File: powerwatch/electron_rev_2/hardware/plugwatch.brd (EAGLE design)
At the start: 57.1 x 93 mm, 111 parts, among them J1 TC2030-JLINK-NL, J2 DM3AT-SF-PEJM5, SW1 SIP3240X, SW2 SIP3240X, SW3 SIP3240X, SW4 SIP3240X, SW7 SIP3240X, U1 MAX-M8, U3 ISL29035, U37 MPU-9250, U4 NRF51822QF, U5 SAFFB1G56KB0F0A, U6 BGA725L6-ALT, U7 OPA322AIDBVT, U8 MAX740XESA, X3 16MHz, X4 ABS05-32.768KHZ-9-T

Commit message: Fixed a schematic boo boo
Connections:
- removed net BLE_VCC: R13.1
- net VCC_BLE: now also R13.1
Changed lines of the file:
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@@
 <wire x1="18.038" y1="9.361" x2="16.727" y2="9.361" width="0.4064" layer="16"/>
 <wire x1="16.727" y1="9.361" x2="16.51" y2="9.144" width="0.4064" layer="16"/>
+<contactref element="R13" pad="1"/>
+<wire x1="16.51" y1="13.716" x2="16.28013125" y2="15.0876" width="0" layer="19" extent="16-16"/>
 </signal>
 <signal name="N$14">
@@
 <wire x1="25.4" y1="36.576" x2="28.575" y2="33.401" width="0.254" layer="1"/>
 </signal>
-<signal name="BLE_VCC">
-<contactref element="R13" pad="1"/>
-</signal>
 <signal name="GND2">

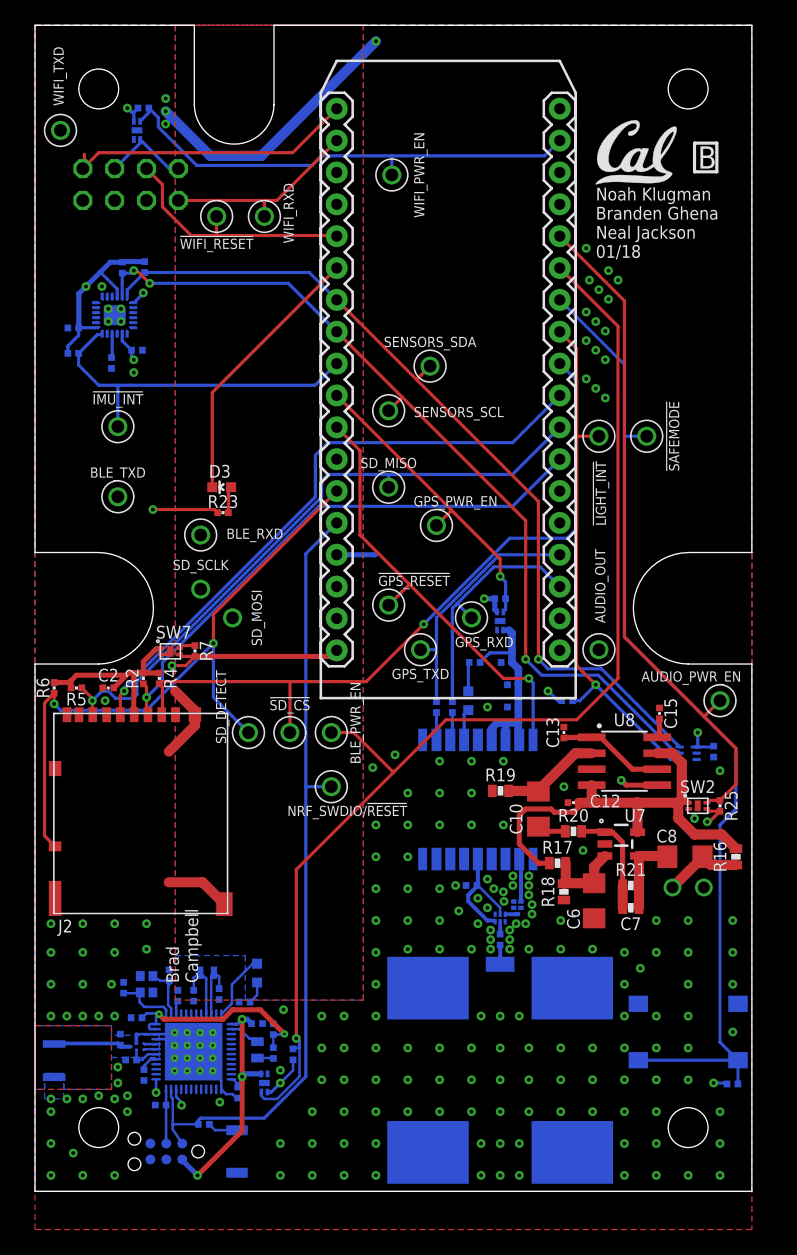
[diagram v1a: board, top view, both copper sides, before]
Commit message: Fix BLE VCC, testpoints, labels, relabel parts
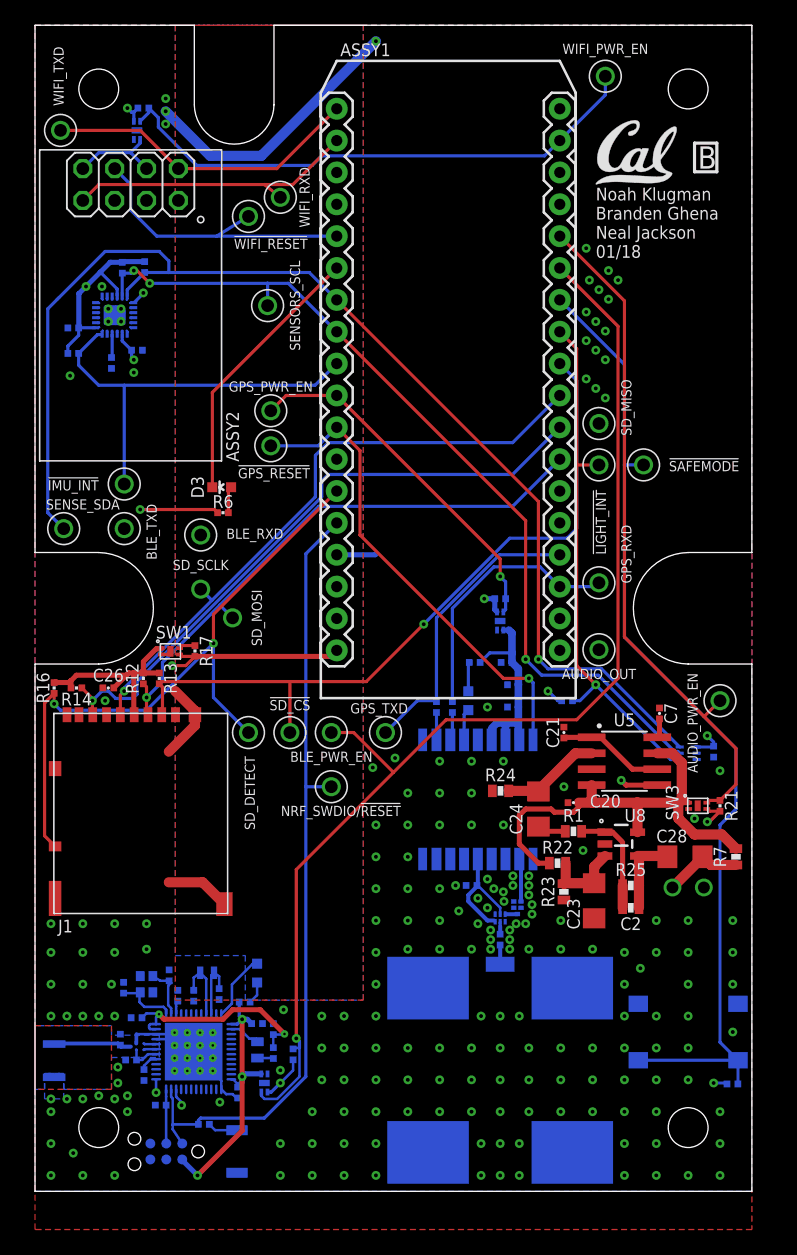
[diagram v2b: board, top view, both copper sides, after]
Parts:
- removed A3: ANT3216A063R2400A, chips:ANT3216A063R2400A
- removed C29: 12pF, passives:0402_CAP
- removed C30: 100nF, passives:0402_CAP
- removed L6: 15nH, passives:0402_CAP
- removed L7: 10uH, passives:0603_CAP
- removed R26: 100k, passives:0402_RES
- removed SW7: SIP3240X, signpost:TDFN4
- removed U37: MPU-9250, Testing:QFN24_PAD
- added ASSY1: ELECTRON, electron:ELECTRON_SINGLE-ROW
- added C16, C17: 100nF, passives:0402_CAP
- added L4, L5: 1k, passives:0402_CAP
- added R22: 100k, passives:0603-RES
- added SW5: SIP3240X, signpost:TDFN4
- added U2: SAFFB1G56KB0F0A, Particle:QCS5I
- A1: value ELECTRON -> ANT3216A063R2400A; device electron:ELECTRON_SINGLE-ROW -> chips:ANT3216A063R2400A
- C1: value 100nF -> 0.8pF
- C10: value 2.2uF -> 2.2nF; device passives:1206 -> passives:0402_CAP
- C12, C13: value 100nF -> 10nF
- C14: value 100nF -> 47nF
- C15: value 330pF -> 100nF
- C19: value 1nF -> 100nF
- C2: value 4.7uF -> 4.4pF; device passives:0402_CAP -> passives:0603_CAP
- C20: value 4.7uF -> 100nF
- C21: value 1uF -> 100nF
- C22: value 12pF -> 1uF
- C23: value 12pF -> 2.2uF; device passives:0402_CAP -> passives:1206
- C24: value 1nF -> 2.2uF; device passives:0402_CAP -> passives:1206
- C25: value 47nF -> 4.7uF
- C26: value 2.2nF -> 4.7uF
- C27: value 0.8pF -> 10uF
- C28: value 12pF -> 10uF; device passives:0402_CAP -> passives:1206
- C3, C5: value 10nF -> 12pF
- C4: value 100nF -> 12pF
- C6: value 2.2uF -> 12pF; device passives:1206 -> passives:0402_CAP
- C7: value 4.4pF -> 330pF; device passives:0603_CAP -> passives:0402_CAP
- C8: value 10uF -> 1nF; device passives:1206 -> passives:0402_CAP
- C9: value 10uF -> 1nF
- J1: value TC2030-JLINK-NL -> DM3AT-SF-PEJM5; device connector:TC2030-IDC-NL -> connector:DM3AT-SF-PEJM5
- J2: value DM3AT-SF-PEJM5 -> TC2030-JLINK-NL; device connector:DM3AT-SF-PEJM5 -> connector:TC2030-IDC-NL
- L2: value 1k -> 10uH; device passives:0402_CAP -> passives:0603_CAP
- L3: value 1k -> 15nH
- R1: value 1k -> 49.9; device passives:0402_RES -> passives:0603-RES
- R12: value 12k -> 10k
- R13: value 1k -> 10k
- R14, R8: value 150 -> 10k
- R15: value 10k -> 12k
- R16: value 3.48k -> 100k; device passives:0603-RES -> passives:0402_RES
- R17, R18, R19: device passives:0603-RES -> passives:0402_RES
- R2: value 10k -> 150
- R20: value 49.9 -> 100k; device passives:0603-RES -> passives:0402_RES
- R21: value 270k -> 100k; device passives:0603-RES -> passives:0402_RES
- R23: value 1k -> 100k; device passives:0402_RES -> passives:0603-RES
- R24: device passives:0402_RES -> passives:0603-RES
- R25: value 100k -> 270k; device passives:0402_RES -> passives:0603-RES
- R3: value 100k -> 150
- R4, R5: value 10k -> 1k
- R6: value 100k -> 1k
- R7: value 100k -> 3.48k; device passives:0402_RES -> passives:0603-RES
- S1: value PTS645SM43SMTR92 -> B3U-1000P; device switches:PTS645 -> switches:B3U-1000P
- S2: value B3U-1000P -> PTS645SM43SMTR92; device switches:B3U-1000P -> switches:PTS645
- U1: value MAX-M8 -> BGA725L6-ALT; device u-blox:MAX-M8 -> Particle:LNA-TSLP-6-2-ALT
- U4: value NRF51822QF -> MAX-M8; device chips:QFN-48-6MM -> u-blox:MAX-M8
- U5: value SAFFB1G56KB0F0A -> MAX740XESA; device Particle:QCS5I -> chips:SOIC-8
- U6: value BGA725L6-ALT -> MPU-9250; device Particle:LNA-TSLP-6-2-ALT -> Testing:QFN24_PAD
- U7: value OPA322AIDBVT -> NRF51822QF; device opamps:SOT23-5 -> chips:QFN-48-6MM
- U8: value MAX740XESA -> OPA322AIDBVT; device chips:SOIC-8 -> opamps:SOT23-5
- moved SW4 76.6 mm to (8.13, 84.6), turned to 0 degrees
- moved SW3 70.0 mm to (52.8, 30.7), flipped to the top, turned to 270 degrees
- moved R19 61.4 mm to (8.64, 86.4), flipped to the bottom
- moved R15 60.3 mm to (10.0, 6.87)
- moved C18 59.0 mm to (6.10, 66.0)
- moved U6 57.0 mm to (6.35, 69.8), turned to 0 degrees
- moved R16 56.0 mm to (1.52, 40.1)
- moved C19 55.2 mm to (3.05, 68.8)
- moved C1 54.0 mm to (6.80, 12.1), turned to 90 degrees
- moved C14 52.2 mm to (8.69, 9.27)
- moved C3 50.8 mm to (7.06, 16.2), turned to 90 degrees
- moved A1 50.6 mm to (1.52, 10.4), flipped to the bottom, turned to 270 degrees
- moved R9 48.3 mm to (8.74, 73.7), turned to 90 degrees
- moved R7 46.1 mm to (55.9, 26.7), turned to 90 degrees
- moved C13 45.7 mm to (8.13, 67.1), flipped to the bottom, turned to 180 degrees
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- renumbered A4 to ASSY2, B2 to B1, X3 to X2, X4 to X1
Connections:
- net !GPS_RESET: now also ASSY1.D4, U4.9; no longer A1.D4, U1.9
- net !IMU_INT: now also ASSY1.D2, R11.1, U6.12; no longer A1.D2, R15.1, U37.12
- net !LIGHT_INT: now also ASSY1.A1, R8.1; no longer A1.A1, R9.1
- net !SAFEMODE: now also ASSY1.A0, R3.2, S2.3, S2.4; no longer A1.A0, R8.2, S1.3, S1.4
- net !SD_CS: now also ASSY1.A2, J1.2, R13.1; no longer A1.A2, J2.2, R4.1
- net !SD_DETECT: now also ASSY1.D6, J1.A, R16.1; no longer A1.D6, J2.A, R6.1
- net !WIFI_RESET: now also ASSY1.C4; no longer A1.C4
- net -AMP: now also C2.1, C28.2, R25.2, U8.4; no longer C7.1, C8.2, R21.2, U7.4
- net AUDIO_OUT: now also ASSY1.B2, U5.5; no longer A1.B2, U8.5
- net AUDIO_PWR_EN: now also ASSY1.B4, R21.1, SW3.4; no longer A1.B4, R25.1, SW2.4
- net AVDD1: now also C22.1, C8.1, L3.1, U7.35, U7.36; no longer C19.1, C21.1, L6.1, U4.35, U4.36
- net A_MIC_OUT: now also C24.1, R24.2, U5.2; no longer C10.1, R19.2, U8.2
- net BLE_PWR_EN: now also ASSY1.B5, R20.1, SW5.4; no longer A1.B5, R24.1, SW4.4
- net BLE_RXD: now also ASSY1.C3, U7.25; no longer A1.C3, U4.25
- net BLE_TXD: now also ASSY1.C2, U7.22; no longer A1.C2, U4.22
- net DCC1: now also L2.2, U7.2; no longer L7.2, U4.2
- net GND: now also A1.S2, ASSY1.GND, ASSY1.GND@2, C10.2, C12.1, C16.2, C17.2, C23.1, C27.1, C4.2, C5.2, C6.2, C7.1, C8.2, C9.2, J1.6, J1.B, J1.MOUNT0, J1.MOUNT1, J1.MOUNT2, J1.MOUNT3, J2.5, R15.2, R23.1, R24.1, S2.2, SW5.2, SW5.PAD, U1.4, U2.2, U2.3, U2.5, U4.1, U4.10, U4.12, U6.11, U6.18, U6.20, U6.9, U6.CENTER, U7.13, U7.33, U7.34, U7.GND, U8.2; no longer A1.GND, A1.GND@2, A3.S2, C12.2, C2.2, C23.2, C24.2, C27.2, C28.2, C29.2, C30.2, C4.1, C5.1, C6.1, C9.1, J1.5, J2.6, J2.B, J2.MOUNT0, J2.MOUNT1, J2.MOUNT2, J2.MOUNT3, R12.2, R18.1, R19.1, S1.2, SW7.2, SW7.PAD, U1.10, U1.12, U37.11, U37.18, U37.20, U37.9, U37.CENTER, U4.13, U4.33, U4.34, U4.GND, U5.2, U5.5, U6.1, U6.4, U7.2, U8.3
- net GPS_PWR_EN: now also ASSY1.D3, R18.1, SW2.4; no longer A1.D3, R3.1, SW1.4
- net GPS_RF_IN: now also U2.4, U4.11; no longer U1.11, U5.4
- net GPS_RXD: now also ASSY1.TX, L5.2; no longer A1.TX, L3.2
- net GPS_TXD: now also ASSY1.RX, L4.2; no longer A1.RX, L2.2
- net GPS_VCC: now also C12.2, C15.2, C27.2, R4.2, SW2.1, U4.6, U4.7, U4.8; no longer C11.2, C4.2, C9.2, R1.2, SW1.1, U1.6, U1.7, U1.8
- net LED: now also ASSY1.C5; no longer A1.C5
- net LNA_IN: now also U1.5; no longer U6.5
- net LNA_OUT: now also U1.3, U2.1; no longer U5.1, U6.3
- net N$1: now also R4.1; no longer R1.1
- net N$10: now also U7.31; no longer U4.31
- net N$11: now also C21.1, U5.1, U5.6; no longer C13.1, U8.1, U8.6
- net N$12: now also U7.32; no longer U4.32
- net N$13: now also A1.S1, C1.1; no longer A3.S1, C27.1
- net N$14: now also SW4.1; no longer SW3.1
- net N$15: now also L2.1, L3.2; no longer L6.2, L7.1
- net N$18: now also C26.1, J1.4, R12.2, R13.2, R14.2, R16.2, SW1.1; no longer C2.1, J2.4, R2.2, R4.2, R5.2, R6.2, SW7.1
- net N$2: now also U4.4; no longer U1.4
- net N$20: now also C3.1, U7.37; no longer C22.1, U4.37
- net N$21: now also C4.1, U7.38; no longer C23.1, U4.38
- net N$22: now also C9.1, U7.39; no longer C24.1, U4.39
- net N$24: now also C14.1, U7.29; no longer C25.1, U4.29
- net N$25: now also R5.2; no longer R13.2
- net N$26: now also R2.2, S1.2; no longer R14.2, S2.2
- net N$3: now also R6.2; no longer R23.2
- net N$4: now also C28.1, R7.1; no longer C8.1, R16.1
- net N$40: now also L4.1, U4.2; no longer L2.1, U1.2
- net N$41: now also L5.1, U4.3; no longer L3.1, U1.3
- net N$5: now also C2.2, R1.2, R25.1, U8.1; no longer C7.2, R20.2, R21.1, U7.1
- net N$6: now also C7.2, U5.8; no longer C15.2, U8.8
- net N$7: now also C24.2, R1.1; no longer C10.2, R20.1
- net N$9: now also C23.2, R22.1, R23.2, U8.3; no longer C6.2, R17.1, R18.2, U7.3
- net NRF_A2: now also C6.1, U7.46; no longer C29.1, U4.46
- net NRF_A3: now also C5.1, U7.45; no longer C28.1, U4.45
- net NRF_P29: now also U7.48; no longer U4.48
- net NRF_SWDCLK: now also J2.4, R15.1, U7.24; no longer J1.4, R12.1, U4.24
- net NRF_SWDIO/!RESET: now also ASSY1.D7, J2.2, R2.1, U7.23; no longer A1.D7, J1.2, R14.1, U4.23
- net REGOUT: now also C18.1, U6.10; no longer C1.1, U37.10
- net SD_ENABLE_POWER: now also R17.1, SW1.4; no longer R7.1, SW7.4
- net SD_MISO: now also ASSY1.A4, J1.7, R14.1; no longer A1.A4, J2.7, R5.1
- net SD_MOSI: now also ASSY1.A5, J1.3, R12.1; no longer A1.A5, J2.3, R2.1
- net SD_SCLK: now also ASSY1.A3, J1.5; no longer A1.A3, J2.5
- net SENSORS_SCL: now also ASSY1.D1, R10.1, U6.23; no longer A1.D1, R11.1, U37.23
- net SENSORS_SDA: now also ASSY1.D0, R9.1, U6.24; no longer A1.D0, R10.1, U37.24
- net VCC: now also ASSY1.3V3, C13.1, C17.1, C19.1, R17.2, R18.2, R19.2, R20.2, R21.2, R3.1, R6.1, R8.2, SW5.3, U6.1, U6.13, U6.22, U6.8; no longer A1.3V3, C14.1, C3.1, C30.1, R15.2, R23.1, R24.2, R25.2, R26.2, R3.2, R7.2, R8.1, SW7.3, U37.1, U37.13, U37.22, U37.8
- net VCC_A_MIC: now also C20.1, R22.2, R7.2, SW3.1, U5.4, U5.7, U8.5; no longer C12.1, R16.2, R17.2, SW2.1, U7.5, U8.4, U8.7
- net VCC_BLE: now also C16.1, C25.1, J2.1, R5.1, SW5.1, U7.1, U7.12; no longer C18.1, C20.1, J1.1, R13.1, SW4.1, U4.1, U4.12
- net VCC_RF: now also C11.2, U1.2, U1.6, U4.14; no longer C5.2, U1.14, U6.2, U6.6
- net VDD_PA1: now also C10.1, U7.30; no longer C26.1, U4.30
- net VIN: now also ASSY1.VIN; no longer A1.VIN
- net WIFI_PWR_EN: now also ASSY1.B1, R19.1, SW4.4; no longer A1.B1, R26.1, SW3.4
- net WIFI_RXD: now also ASSY1.C1; no longer A1.C1
- net WIFI_TXD: now also ASSY1.C0; no longer A1.C0
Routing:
- net SENSORS_SDA: track 69.9 -> 99.9 mm
- net WIFI_RXD: track 15.9 -> 23.8 mm
- net WIFI_PWR_EN: track 38.8 -> 43.9 mm
- net !IMU_INT: track 28.7 -> 33.3 mm
- net !WIFI_RESET: track 20.0 -> 24.1 mm
- net GPS_PWR_EN: track 24.6 -> 28.7 mm
- net GPS_TXD: track 19.9 -> 23.7 mm
- net !GPS_RESET: track 34.9 -> 38.5 mm
- net SD_MISO: track 51.6 -> 53.9 mm
- net WIFI_TXD: track 23.2 -> 25.3 mm
- net AUDIO_OUT: track 55.6 -> 57.4 mm
- net GPS_RXD: track 19.6 -> 21.3 mm
- net VCC_BLE: track 21.3 -> 22.8 mm
- net SD_MOSI: track 44.3 -> 45.8 mm
- net SD_SCLK: track 48.6 -> 49.8 mm
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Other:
- board text added: "SENSE_SDA"
- board text removed: "Brad Campbell"
- board text removed: "SENSORS_SDA"

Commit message: Fix BOM issues
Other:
- board text added: ">REV"
- board text removed: "B"
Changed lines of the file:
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@@
 Neal Jackson
 01/18</text>
-<text x="52.832" y="81.534" size="1.778" layer="25" font="vector" ratio="12">B</text>
+<text x="52.832" y="81.534" size="1.778" layer="25" font="vector" ratio="12">&gt;REV</text>
 <wire x1="52.578" y1="81.28" x2="54.356" y2="81.28" width="0.254" layer="25"/>
 <wire x1="54.356" y1="81.28" x2="54.356" y2="83.566" width="0.254" layer="25"/>
@@
 </plain>
 <attributes>
+<attribute name="REV" value="B"/>
 </attributes>
 <variantdefs>
@@
 <element name="C17" library="passives" package="0402_CAP" value="100nF" x="54.102" y="35.052" smashed="yes" rot="MR270">
 <attribute name="DIGIKEY" value="490-10777-1-ND" x="50.4444" y="34.1122" size="1.778" layer="28" rot="MR270" display="off"/>
-<attribute name="MPN" value="MF-CAP-0402-0.1uF" x="50.4444" y="34.1122" size="1.778" layer="28" rot="MR270" display="off"/>
-<attribute name="MPN1" value="GRM155R71A104JA01D" x="50.4444" y="34.1122" size="1.778" layer="28" rot="MR270" display="off"/>
 <attribute name="NAME" x="54.737" y="35.052" size="1.016" layer="26" font="vector" ratio="12" rot="MR90" align="bottom-center"/>
 </element>
@@
 <element name="C20" library="passives" package="0402_CAP" value="100nF" x="42.926" y="30.988" smashed="yes" rot="R180">
 <attribute name="DIGIKEY" value="490-10777-1-ND" x="42.926" y="30.988" size="1.778" layer="27" rot="R180" display="off"/>
-<attribute name="MPN" value="MF-CAP-0402-0.1uF" x="42.926" y="30.988" size="1.778" layer="27" rot="R180" display="off"/>
-<attribute name="MPN1" value="GRM155R71A104JA01D" x="42.926" y="30.988" size="1.778" layer="27" rot="R180" display="off"/>
 <attribute name="NAME" x="45.466" y="30.607" size="1.016" layer="25" font="vector" ratio="12" align="bottom-center"/>
 </element>
 <element name="C21" library="passives" package="0402_CAP" value="100nF" x="42.164" y="36.576" smashed="yes" rot="R90">
 <attribute name="DIGIKEY" value="490-10777-1-ND" x="42.164" y="36.576" size="1.778" layer="27" rot="R90" display="off"/>
-<attribute name="MPN" value="MF-CAP-0402-0.1uF" x="42.164" y="36.576" size="1.778" layer="27" rot="R90" display="off"/>
-<attribute name="MPN1" value="GRM155R71A104JA01D" x="42.164" y="36.576" size="1.778" layer="27" rot="R90" display="off"/>
 <attribute name="NAME" x="41.783" y="36.576" size="1.016" layer="25" font="vector" ratio="12" rot="R90" align="bottom-center"/>
 </element>
@@
 </element>
 <element name="D2" library="leds" package="LED-0603" value="LED0603" x="17.7038" y="17.399" smashed="yes" rot="MR0">
+<attribute name="DIGIKEY" value="160-1837-6-ND" x="17.7038" y="17.399" size="1.778" layer="28" rot="MR0" display="off"/>
 <attribute name="NAME" x="18.4023" y="17.399" size="1.016" layer="26" font="vector" ratio="12" rot="MR90" align="bottom-center"/>
 <attribute name="VALUE" x="16.8783" y="17.399" size="1.016" layer="28" font="vector" ratio="12" rot="MR90" align="top-center"/>
@@
 </element>
 <element name="D3" library="leds" package="LED-0603" value="LED0603" x="14.8844" y="56.134" locked="yes" smashed="yes" rot="R90">
+<attribute name="DIGIKEY" value="160-1837-6-ND" x="14.8844" y="56.134" size="1.778" layer="27" rot="R90" display="off"/>
 <attribute name="NAME" x="13.462" y="56.134" size="1.016" layer="25" font="vector" ratio="12" rot="R90" align="bottom-center"/>
 <attribute name="VALUE" x="14.8844" y="56.9595" size="1.016" layer="27" font="vector" ratio="12" rot="R180" align="top-center"/>

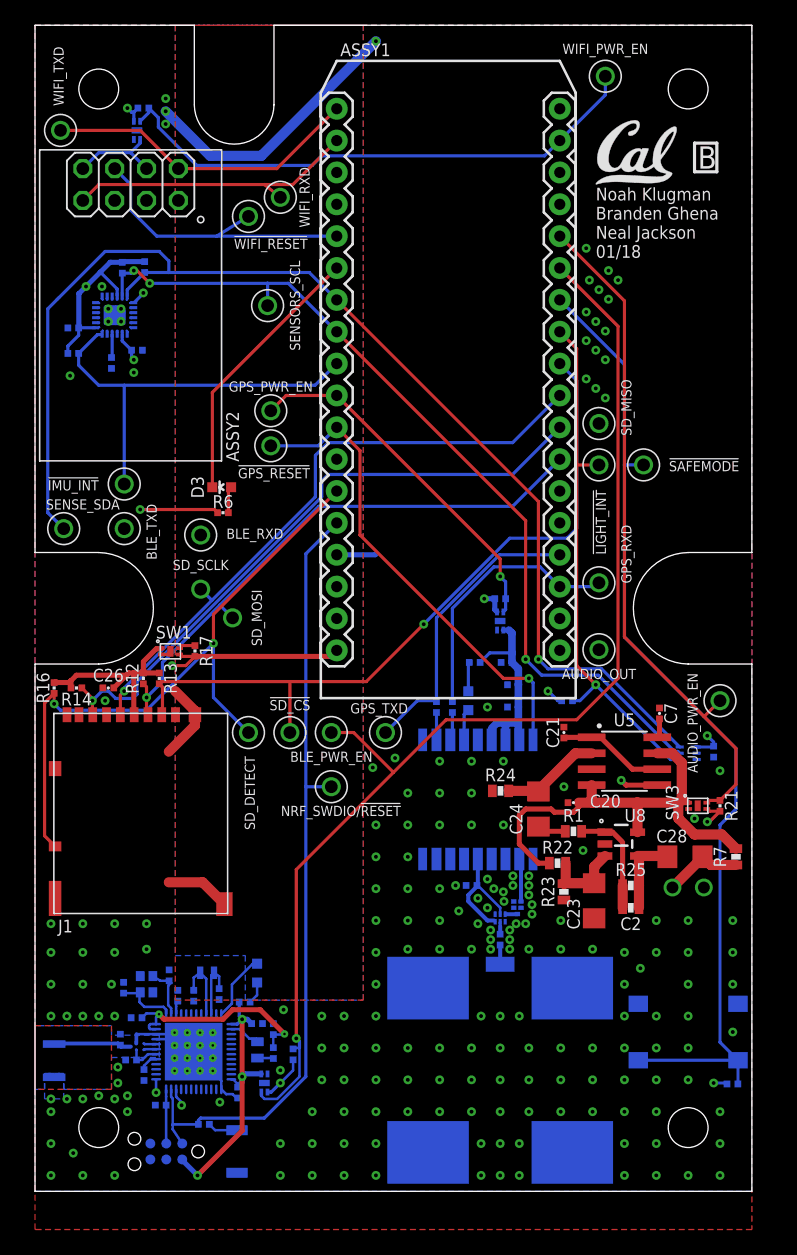
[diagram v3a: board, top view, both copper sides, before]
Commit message: add the fixed power switch
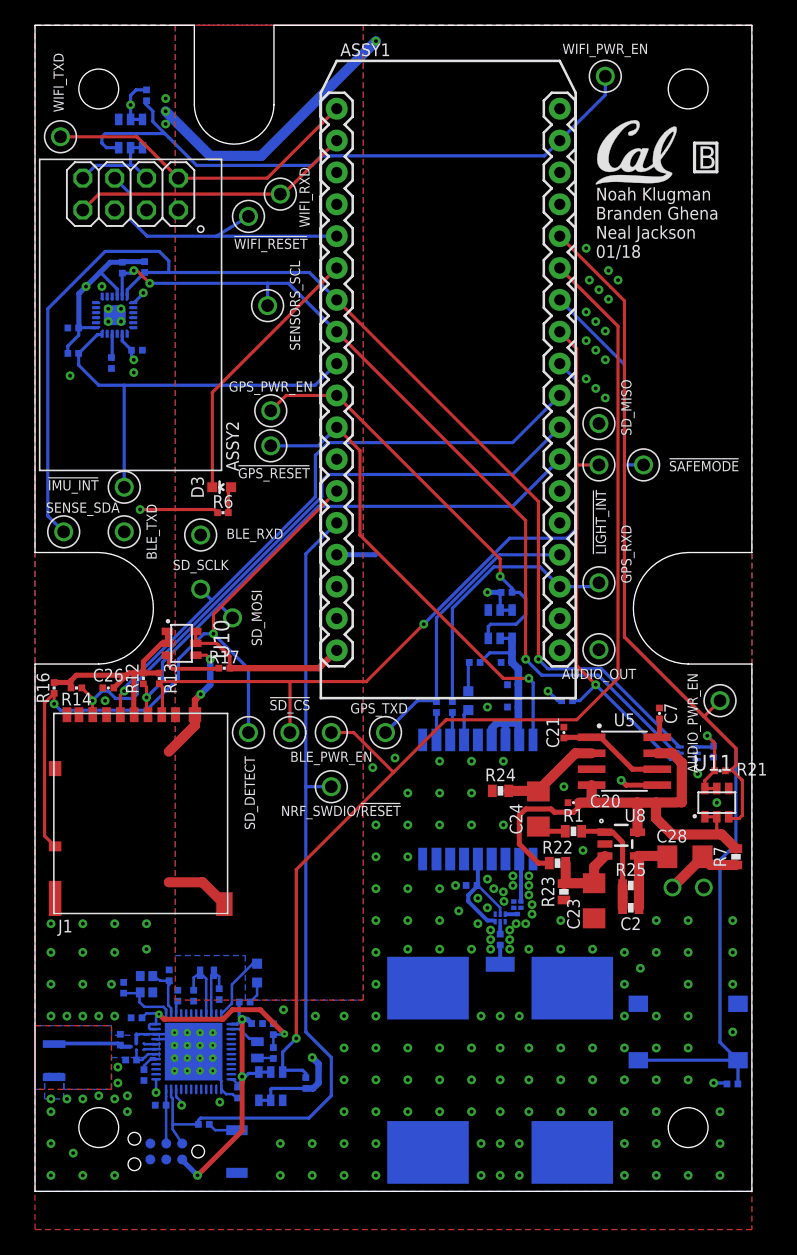
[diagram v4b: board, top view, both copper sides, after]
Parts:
- removed SW1, SW2, SW3, SW5: SIP3240X, signpost:TDFN4
- added U$5, U10, U11, U9: SIP32510, chips:TSOT23-6
- SW4: value SIP3240X -> SIP32510; device signpost:TDFN4 -> chips:TSOT23-6
- moved R21 2.79 mm to (54.6, 33.5), turned to 180 degrees
- moved R17 2.71 mm to (15.1, 41.7), turned to 0 degrees
- moved R20 2.50 mm to (21.6, 8.64)
- moved R19 1.05 mm to (8.89, 87.4), turned to 90 degrees
- moved ASSY2 0.76 mm to (7.62, 79.5)
- moved R18 0.72 mm to (37.6, 47.8)
- moved SW4 0.57 mm to (7.62, 84.3)
- moved TP13 0.51 mm to (2.03, 84.1)
- moved TP15 0.25 mm to (7.11, 52.6)
- moved TP19 0.25 mm to (2.29, 52.6)
- moved TP21 0.25 mm to (7.11, 56.1)
- moved TP14 0.25 mm to (19.6, 79.5)
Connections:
- net AUDIO_PWR_EN: now also U11.3; no longer SW3.4
- net BLE_PWR_EN: now also U9.3; no longer SW5.4
- net GND: now also SW4.4, U$5.4, U10.4, U11.4, U9.4; no longer SW1.2, SW1.PAD, SW2.2, SW2.PAD, SW3.2, SW3.PAD, SW4.2, SW4.PAD, SW5.2, SW5.PAD
- net GPS_PWR_EN: now also U$5.3; no longer SW2.4
- net GPS_VCC: now also U$5.1, U$5.2; no longer SW2.1
- net N$14: now also SW4.2
- net N$18: now also U10.1, U10.2; no longer SW1.1
- net SD_ENABLE_POWER: now also U10.3; no longer SW1.4
- net VCC: now also SW4.5, SW4.6, U$5.5, U$5.6, U10.5, U10.6, U11.5, U11.6, U9.5, U9.6; no longer SW1.3, SW2.3, SW3.3, SW4.3, SW5.3
- net VCC_A_MIC: now also U11.1, U11.2; no longer SW3.1
- net VCC_BLE: now also U9.1, U9.2; no longer SW5.1
- net WIFI_PWR_EN: now also SW4.3; no longer SW4.4
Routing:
- net VCC: track 75.3 -> 91.0 mm, vias 12 -> 10
- net WIFI_PWR_EN: track 43.9 -> 50.4 mm
- net GPS_PWR_EN: track 28.7 -> 34.1 mm
- net NRF_SWDIO/!RESET: track 64.2 -> 68.0 mm
- net SD_ENABLE_POWER: track 1.32 -> 4.97 mm
- net VCC_A_MIC: track 35.8 -> 39.5 mm
- net GND: track 48.8 -> 52.0 mm, vias 213 -> 211
- net BLE_PWR_EN: track 94.2 -> 91.8 mm
- net AUDIO_PWR_EN: track 54.3 -> 56.1 mm
- net N$18: track 16.9 -> 18.5 mm
- net WIFI_RXD: track 23.8 -> 22.5 mm
- net !SD_DETECT: track 53.3 -> 54.5 mm
- net BLE_RXD: track 81.2 -> 80.4 mm
- net VCC_BLE: track 22.8 -> 23.6 mm
- net N$14: track 7.50 -> 8.29 mm

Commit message: fix up silkscreen
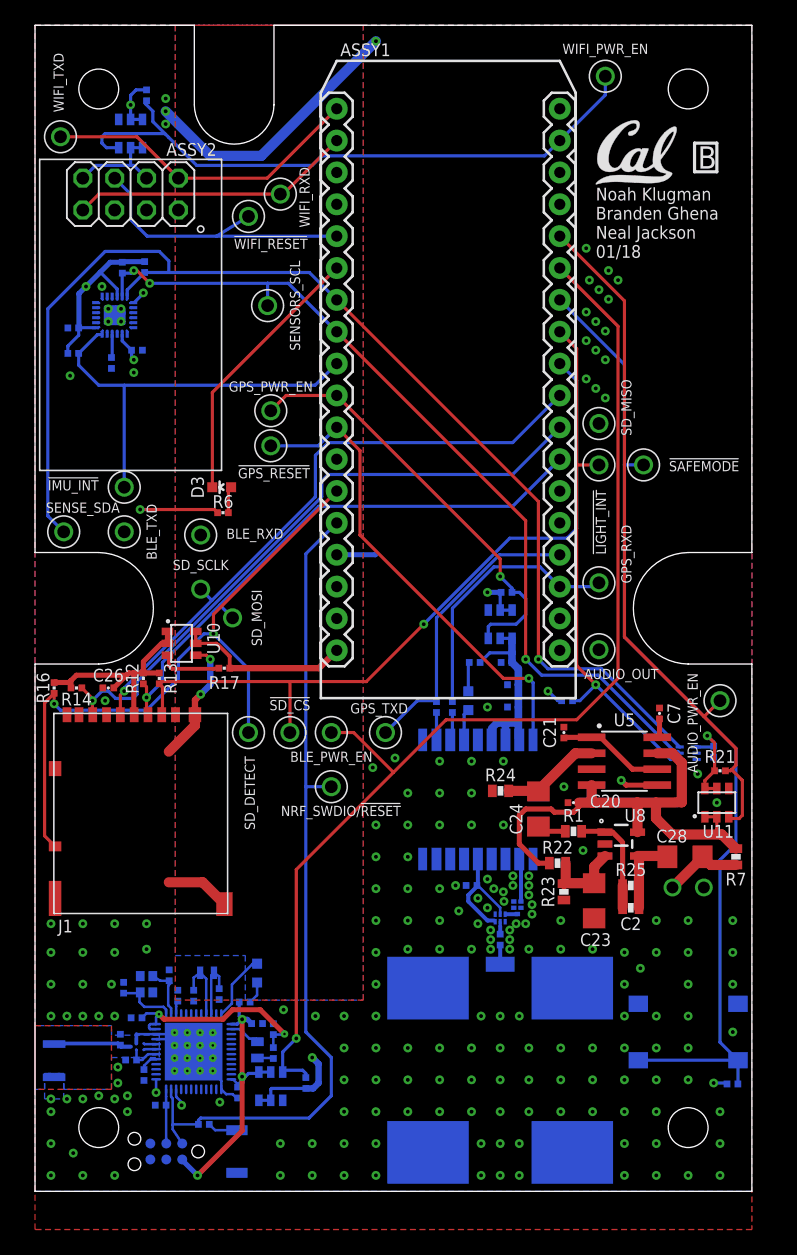
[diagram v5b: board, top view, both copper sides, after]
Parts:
- renumbered U$5 to U12
